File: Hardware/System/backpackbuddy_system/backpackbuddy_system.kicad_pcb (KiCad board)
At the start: 2 copper layers, 65 x 56 mm, 88 parts, among them J1 PIR, J10 USB_B_Micro, J11 Battery, J2 Ultrasonic 2, J3 Ultrasonic 1, J4 L_Vibes, J5 Left Vibration 2, J6 RPi_GPIO, J7 ESP8266, J8 R_Vibes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

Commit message: gerbers
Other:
- board text added: "Backpack Buddy Jeric,Emily,Rahul 3/2023"

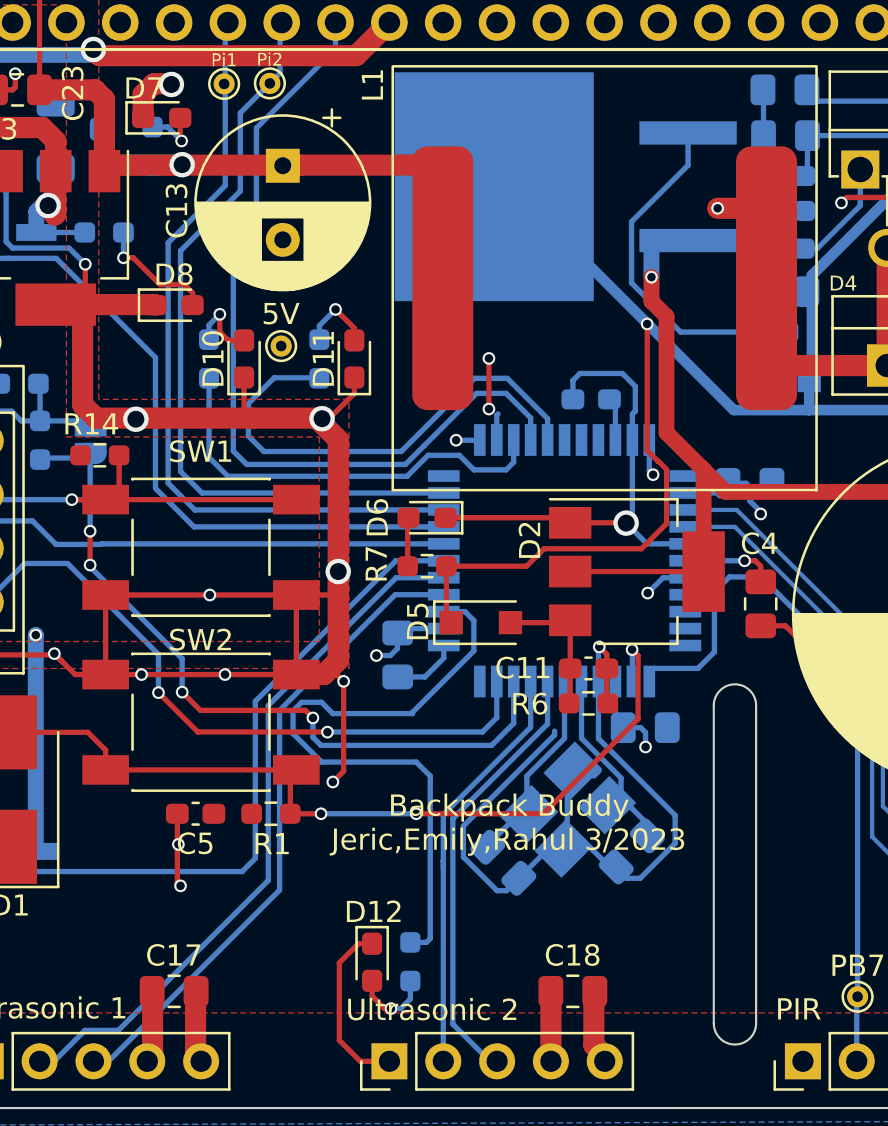
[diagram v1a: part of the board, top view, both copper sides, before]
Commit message: updated silkscreen
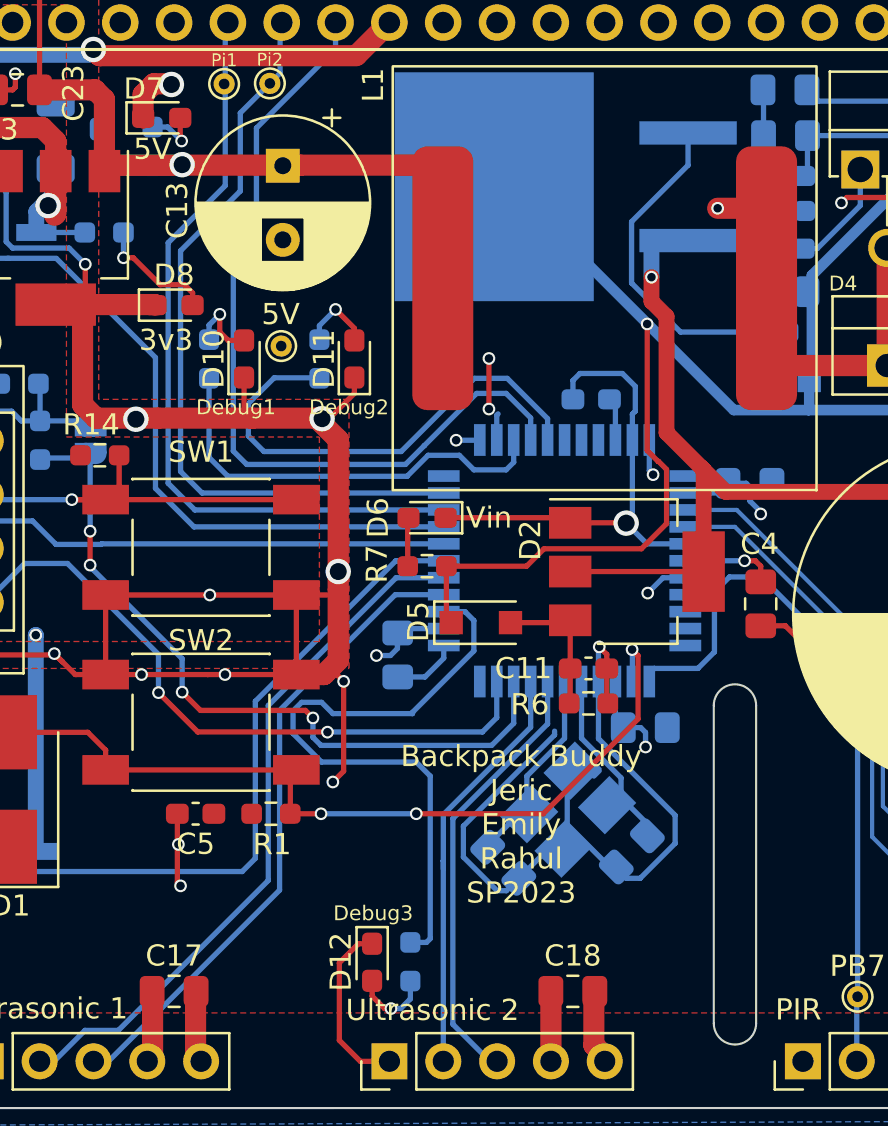
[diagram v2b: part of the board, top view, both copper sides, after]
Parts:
- D10: value Green -> Debug1
- D11: value Yellow -> Debug2
- D12: value Amber -> Debug3
- D6: value Red -> Vin
- D7: value Red -> 5V
- D8: value Red -> 3v3
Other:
- board text added: "Backpack Buddy Jeric Emily Rahul SP2023"
- board text removed: "Backpack Buddy Jeric,Emily,Rahul 3/2023"
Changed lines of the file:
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@@
     (pad_to_mask_clearance 0)
     (pcbplotparams
-      (layerselection 0x0001030_ffffffff)
+      (layerselection 0x00010f0_ffffffff)
       (disableapertmacros false)
       (usegerberextensions false)
@@
       (effects (font (size 1 1) (thickness 0.15)))
     )
-    (fp_text value "Red" (at 0 1.43) (layer "F.Fab")
+    (fp_text value "5V" (at -0.4318 1.4732) (layer "F.SilkS")
       (effects (font (size 1 1) (thickness 0.15)))
     )
@@
       (effects (font (size 1 1) (thickness 0.15)))
     )
-    (fp_text value "Red" (at 0 1.43) (layer "F.Fab")
+    (fp_text value "Vin" (at -2.921 0) (layer "F.SilkS")
       (effects (font (size 1 1) (thickness 0.15)))
     )
@@
       (effects (font (size 1 1) (thickness 0.15)))
     )
-    (fp_text value "Red" (at 0 1.43) (layer "F.Fab")
+    (fp_text value "3v3" (at -0.381 1.651) (layer "F.SilkS")
       (effects (font (size 1 1) (thickness 0.15)))
     )
@@
       (effects (font (size 1 1) (thickness 0.15)))
     )
-    (fp_text value "Yellow" (at 0 1.43 90) (layer "F.Fab")
-      (effects (font (size 1 1) (thickness 0.15)))
+    (fp_text value "Debug2" (at -2.286 -0.254 180) (layer "F.SilkS")
+      (effects (font (size 0.7 0.7) (thickness 0.15)))
     )
     (fp_text user "${REFERENCE}" (at 0 0 90) (layer "F.Fab")
@@
       (effects (font (size 1 1) (thickness 0.15)))
     )
-    (fp_text value "Green" (at 0 1.43 90) (layer "F.Fab")
-      (effects (font (size 1 1) (thickness 0.15)))
+    (fp_text value "Debug1" (at -2.286 -0.381 180) (layer "F.SilkS")
+      (effects (font (size 0.7 0.7) (thickness 0.15)))
     )
     (fp_text user "${REFERENCE}" (at 0 0 90) (layer "F.Fab")
@@
     (property "Stock" "https://www.digikey.com/en/products/detail/w%C3%BCrth-elektronik/150060AS75000/10468330?utm_adgroup=LED%20Indication%20-%20Discrete&utm_source=google&utm_medium=cpc&utm_campaign=Shopping_Product_Optoelectronics_NEW&utm_term=&utm_content=LED%20Indication%20-%20Discrete")
     (attr smd)
-    (fp_text reference "D12" (at -2.3622 -0.0762 180) (layer "F.SilkS")
+    (fp_text reference "D12" (at -0.0254 1.4732 -90) (layer "F.SilkS")
       (effects (font (size 1 1) (thickness 0.15)))
     )
-    (fp_text value "Amber" (at 0 1.43 90) (layer "F.Fab")
-      (effects (font (size 1 1) (thickness 0.15)))
+    (fp_text value "Debug3" (at -2.3114 -0.0508 180) (layer "F.SilkS")
+      (effects (font (size 0.7 0.7) (thickness 0.15)))
     )
     (fp_text user "${REFERENCE}" (at 0 0 90) (layer "F.Fab")
@@
   (gr_line (start 176.036937 62.995948) (end 176.009999 113.03) (layer "Edge.Cuts") (width 0.1))
   (gr_arc (start 155.01 97) (mid 156.01 96) (end 157.01 97) (layer "Edge.Cuts") (width 0.1))
-  (gr_text "Backpack Buddy\nJeric,Emily,Rahul 3/2023" (at 145.3388 102.5398) (layer "F.SilkS")
+  (gr_text "Backpack Buddy\nJeric\nEmily\nRahul\nSP2023" (at 145.923 102.616) (layer "F.SilkS")
     (effects (font (size 1 1) (thickness 0.15)))
   )

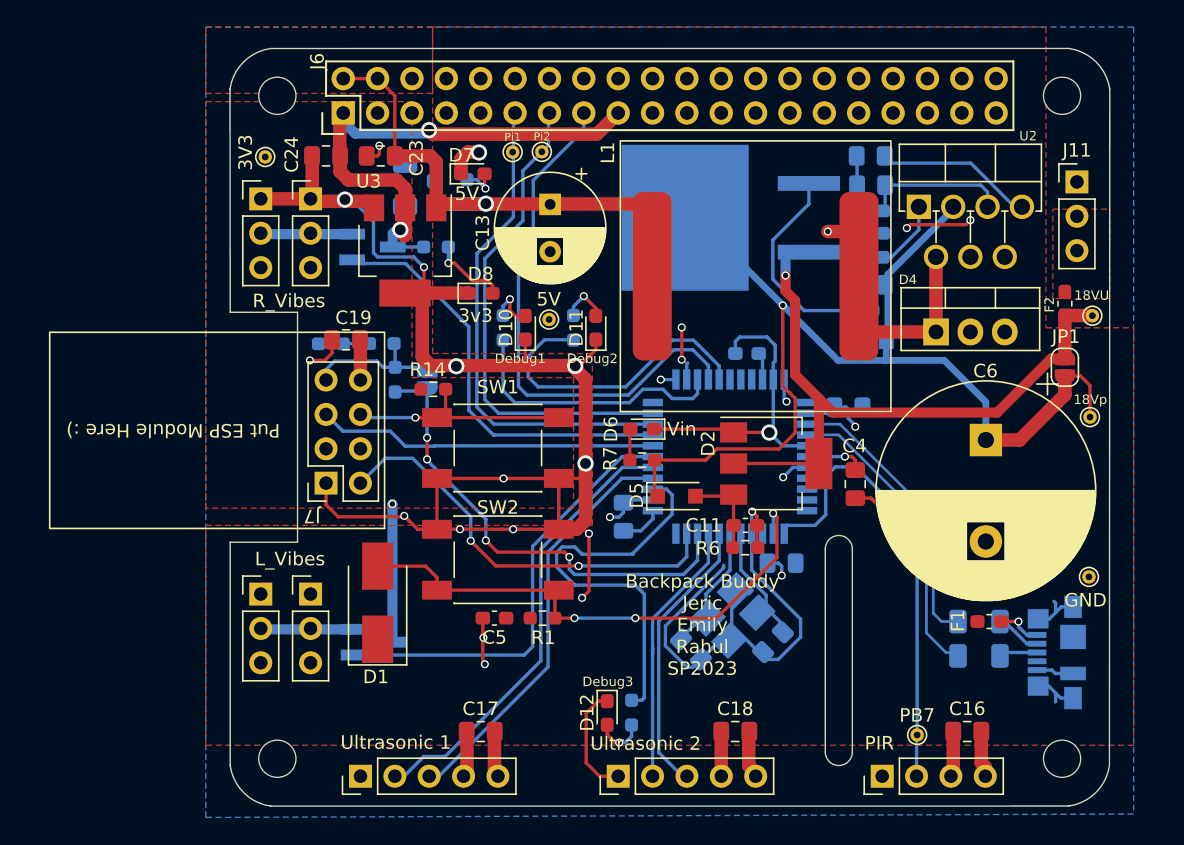
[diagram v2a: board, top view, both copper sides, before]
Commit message: Board run 2 start -> rewire arduino connections
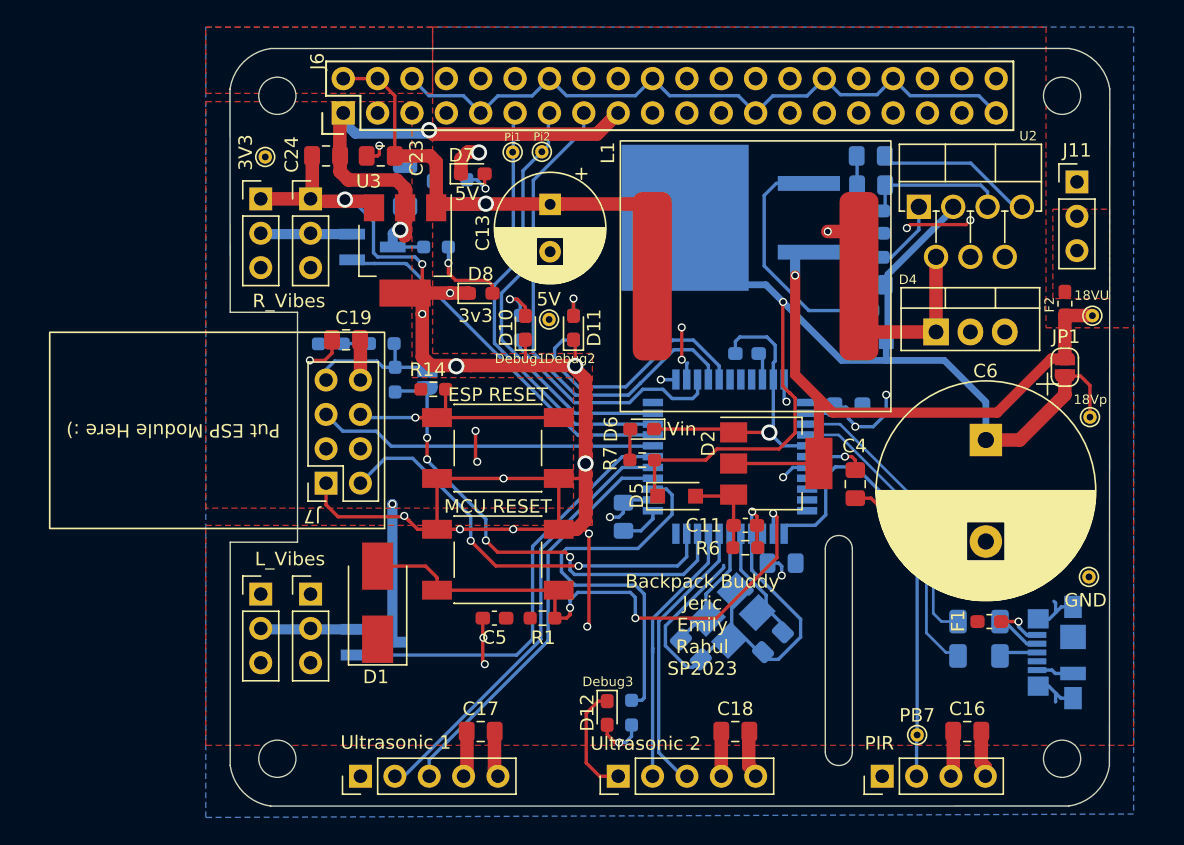
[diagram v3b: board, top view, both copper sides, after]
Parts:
- SW1: value ESP8266 RESET -> ESP RESET
- moved D11 1.65 mm to (136.4, 80.6)
- moved R11 1.27 mm to (132.5, 80.6)
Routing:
- net GND: track 230.3 -> 284.2 mm, vias 23 -> 27
- net /Raspberry Pi/GPIO17: track 36.4 -> 31.8 mm
- net /Raspberry Pi/GPIO27: track 36.0 -> 31.7 mm
- net /microcontroller/PF5: track 23.0 -> 18.9 mm
- net +5V: track 67.8 -> 71.9 mm, vias 7 -> 8
- net /microcontroller/PB6: track 30.5 -> 26.9 mm
- net /microcontroller/~{RESET}: track 40.0 -> 43.1 mm
- net /microcontroller/PF7: track 20.4 -> 17.3 mm
- net /Raspberry Pi/GPIO22: track 39.4 -> 36.4 mm
- net Net-(D3-Pad2): track 17.0 -> 18.7 mm
- net Net-(D2-Pad2): track 50.3 -> 49.2 mm
- net /Power/18V PROTECTED: track 81.9 -> 83.0 mm
- net Net-(D11-Pad2): track 3.57 -> 2.53 mm
- net /microcontroller/PD4: track 30.3 -> 29.3 mm
- net /microcontroller/PD7: track 33.4 -> 32.4 mm

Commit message: pcb redone
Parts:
- removed TP7: Pi1, TestPoint:TestPoint_THTPad_D1.0mm_Drill0.5mm
- removed TP8: Pi2, TestPoint:TestPoint_THTPad_D1.0mm_Drill0.5mm
- D10: value Debug1 -> DB1
- D11: value Debug2 -> DB2
- D12: value Debug3 -> DB3
- D6: value Vin -> Red
- D7: value 5V -> 5v
- H1, H2, H3, H4: value (none) -> MountingHole
- J4: value L_Vibes -> Left Vibes
- J8: value R_Vibes -> Right Vibes
- TP1: value 18VU -> 9V Unprotected
- TP3: value 18Vp -> Protected 9V
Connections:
- J2 pad 2: /microcontroller/PD1 -> /microcontroller/PC6
- J2 pad 3: /microcontroller/PD0 -> /microcontroller/PC7
- U1 pad 18: /microcontroller/PD0 -> /Raspberry Pi/GPIO3_SCL
- U1 pad 19: /microcontroller/PD1 -> /Raspberry Pi/GPIO2_SDA
- U1 pad 31: /Raspberry Pi/GPIO17 -> /microcontroller/PC6
- U1 pad 32: /Raspberry Pi/GPIO27 -> /microcontroller/PC7
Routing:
- net /Raspberry Pi/GPIO2_SDA: track 0.00 -> 48.8 mm, vias 0 -> 2
- net /Raspberry Pi/GPIO3_SCL: track 0.00 -> 47.6 mm, vias 0 -> 2
- net /Raspberry Pi/GPIO17: track 31.8 -> 0.00 mm
- net /Raspberry Pi/GPIO27: track 31.7 -> 0.00 mm
- net /microcontroller/PC7: track 0.00 -> 31.3 mm, vias 0 -> 2
- net /microcontroller/PC6: track 0.00 -> 28.8 mm, vias 0 -> 2
- net /microcontroller/PD0: track 20.8 -> 0.00 mm
- net /microcontroller/PD1: track 20.0 -> 0.00 mm
- net +5V: track 71.9 -> 65.6 mm
- net +3V3: track 54.1 -> 51.7 mm, vias 3 -> 2
- net GND: track 284.2 -> 285.9 mm
- net Net-(D10-Pad2): track 3.80 -> 2.59 mm

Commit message: updated thing
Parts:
- D6: value Red -> VinP
- TP1: value 9V Unprotected -> VinU
- TP3: value Protected 9V -> VinP
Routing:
- net GND: track 285.9 -> 286.6 mm

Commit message: version 3 board
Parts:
- added J12: ICSP, Connector_PinHeader_2.54mm:PinHeader_2x03_P2.54mm_Vertical, B.Cu at (162.4, 107.9)
- D10: value DB1 -> Green
- D11: value DB2 -> Yellow
- D12: value DB3 -> Amber
- D6: value VinP -> Red
- D7: value 5v -> Red
- D8: value 3v3 -> Red
- J4: value Left Vibes -> Left Vibration 1
- J8: value Right Vibes -> Right Vibration 1
- SW1: value ESP RESET -> ESP8266 RESET
- TP1: value VinU -> 9V Unprotected
- TP3: value VinP -> Protected 9V
- U2: footprint Package_TO_SOT_THT:TO-220F-7_P2.54x3.7mm_StaggerEven_Lead3.5mm_Vertical -> Package_TO_SOT_THT:TO-220F-7_P2.54x3.7mm_StaggerOdd_Lead3.5mm_Vertical
- moved C16 5.34 mm to (165.6, 105.2)
- moved U2 4.05 mm to (162.1, 75.8)
- moved PB7 2.17 mm to (159.9, 109.6)
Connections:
- net /microcontroller/~{RESET} renamed /RESET
- D4 pad 1: Net-(C12-Pad2) -> GND
- D4 pad 2: GND -> Net-(C12-Pad2)
- D4 pad 3: (no net) -> GND
- U1 pad 10: /microcontroller/PB2 -> /MOSI
- U1 pad 11: /microcontroller/PB3 -> /MISO
- U1 pad 9: /microcontroller/PB1 -> /SCLK
- U3 pad 2: +3V3 -> GND
- U3 pad 3: GND -> +3V3
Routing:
- net /RESET: track 43.1 -> 78.1 mm
- net /MOSI: track 0.00 -> 25.1 mm
- net /SCLK: track 0.00 -> 23.3 mm
- net /MISO: track 0.00 -> 20.8 mm
- net +5V: track 65.6 -> 75.7 mm
- net Net-(C12-Pad2): track 23.4 -> 32.9 mm
- net GND: track 286.6 -> 295.1 mm, vias 27 -> 26
- net /microcontroller/PB7: track 34.0 -> 27.2 mm
- net Net-(C8-Pad1): track 11.7 -> 16.4 mm
- net Net-(C10-Pad1): track 10.9 -> 15.4 mm
- net +3V3: track 51.7 -> 47.4 mm
- net Net-(C12-Pad1): track 5.24 -> 2.99 mm
- net /Power/18V PROTECTED: track 83.0 -> 81.5 mm
